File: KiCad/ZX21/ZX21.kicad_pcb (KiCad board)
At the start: 2 copper layers, 142 x 100 mm, 131 parts, among them IC1 ULA 2C210E, IC101 555, IC102 74HCT00, IC2 AT28C256, IC3 Z80A, IC301 3V3 PSU, IC302 ESP32-WROOM, IC303 AZ1117-3.3, IC4 62256, IC501 YM2149, IC502 GAL16V8, IC503 YMZ284, IC801 AS6C4008Extra, J1 Jack-DC, J101 Conn_01x03, J203 Conn_01x03, J204 Conn_01x03, J301 Conn_01x04, J302 Conn_01x03, J401 DB9_Male, J501 Conn_01x06, J502 Conn_01x08, J503 Conn_01x08, J504 Conn_01x08, J601 Conn_02x08_Odd_Even, J701 Conn_02x23_Row_Letter_First, J702 Conn_01x09, J703 Conn_01x09, X1 3.5MHz

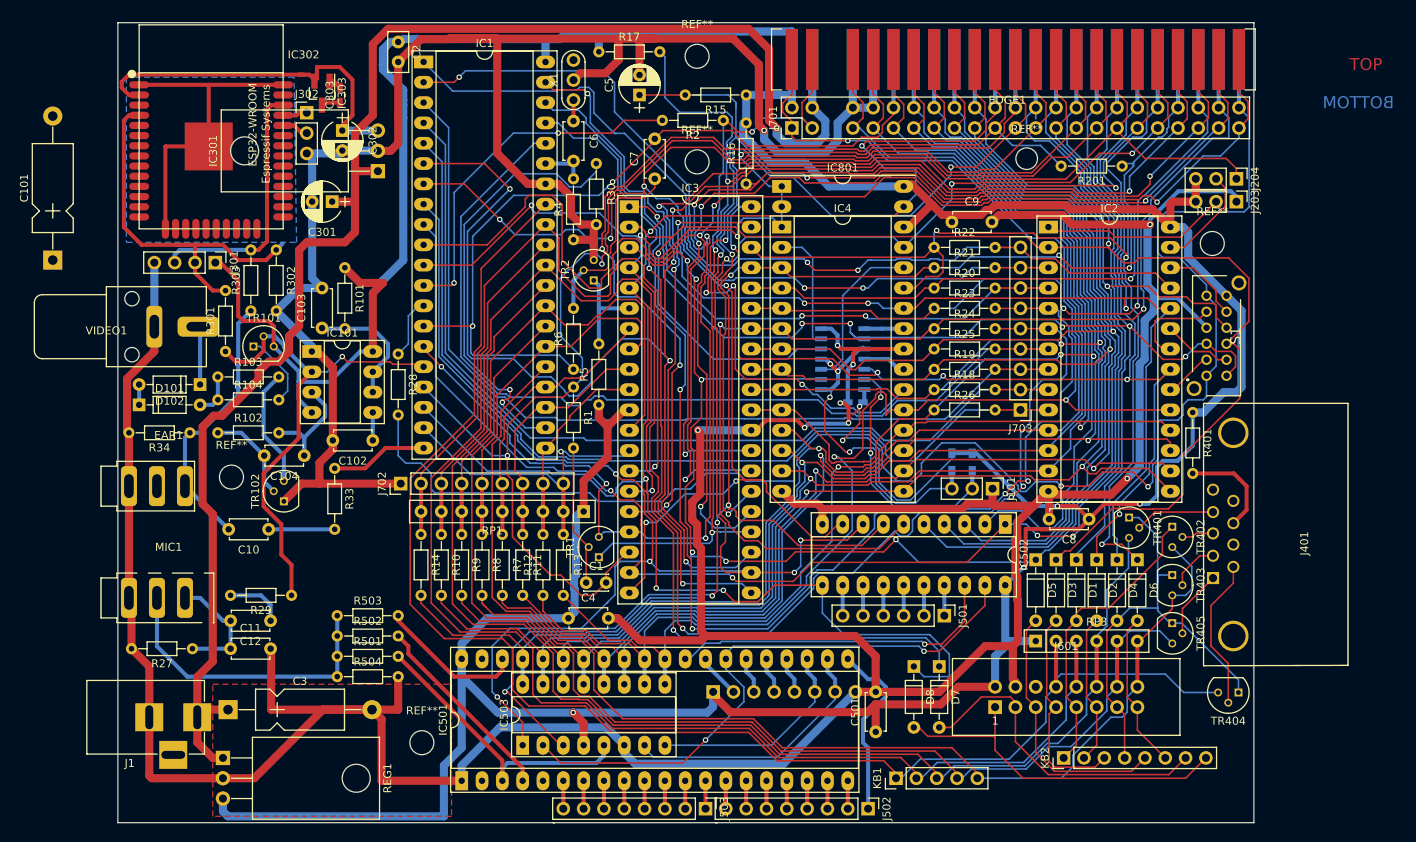
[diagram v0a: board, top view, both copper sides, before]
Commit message: ESP32 Flipped
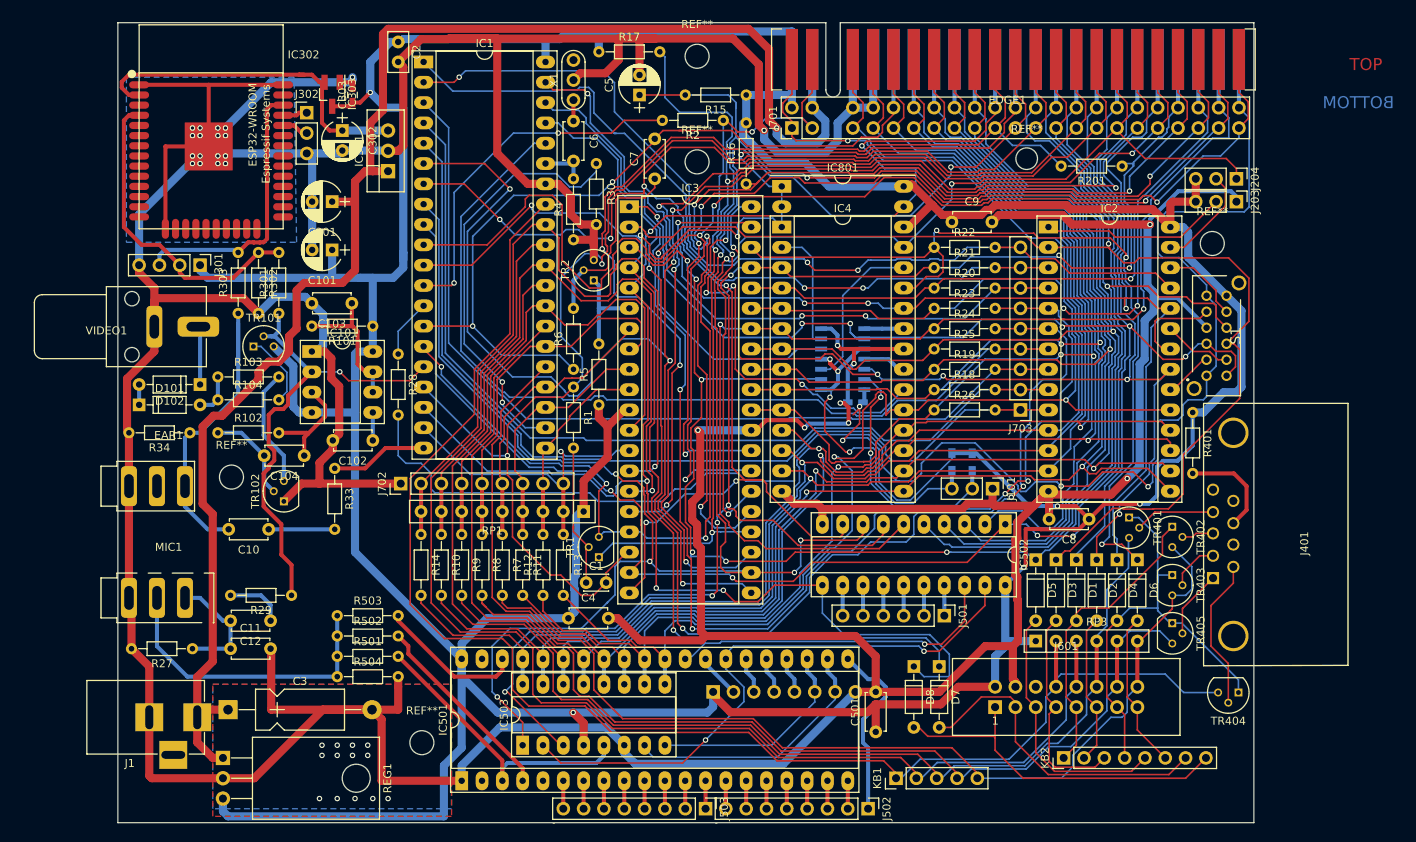
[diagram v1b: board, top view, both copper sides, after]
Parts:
- C101: footprint Capacitors_ThroughHole:CP_Axial_L11.0mm_D5.0mm_P18.00mm_Horizontal -> Capacitors_ThroughHole:CP_Radial_D5.0mm_P2.50mm
- IC301: footprint TO_SOT_Packages_THT:TO-220-3_Horizontal -> TO_SOT_Packages_THT:TO-220-3_Vertical
- moved C101 34.9 mm to (57.8, 65.4), turned to 180 degrees
- moved R301 8.19 mm to (51.1, 73.3)
- moved R101 8.09 mm to (62.9, 74.9), turned to 180 degrees
- moved C103 4.85 mm to (60.2, 72.1), turned to 180 degrees
- moved R302 2.25 mm to (48.6, 65.7)
- moved J301 1.93 mm to (41.3, 67.3)
- moved R303 1.62 mm to (46.0, 73.3)
- moved C303 1.59 mm to (60.3, 46.0)
- moved IC303 1.28 mm to (57.8, 46.0)
- moved IC301 1.27 mm to (64.8, 55.6)
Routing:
- net GND: track 775.2 -> 839.0 mm, vias 9 -> 39
- net +5V: track 562.4 -> 620.2 mm, vias 6 -> 7
- net VP: track 48.4 -> 39.4 mm
- net Net-(C103-Pad1): track 15.9 -> 22.8 mm
- net EAR_IN: track 33.8 -> 38.7 mm
- net TAPE_OUT: track 63.2 -> 59.9 mm
- net +3V3: track 47.1 -> 43.9 mm
- net A13: track 202.8 -> 200.1 mm
- net CLK: track 103.3 -> 101.0 mm
- net Net-(IC1-Pad22): track 54.7 -> 52.7 mm
- net Net-(C104-Pad1): track 15.5 -> 13.5 mm
- net RD: track 198.0 -> 196.4 mm
- net WR: track 265.3 -> 266.6 mm
- net IO22: track 33.0 -> 34.3 mm
- net D3: track 44.8 -> 45.9 mm
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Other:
- outline, holes or cut-outs redrawn
- rule trace_min: 0 -> 0.2032

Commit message: Gerbers made
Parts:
- added REF***: OSHW-Logo2_7.3x6mm_SilkScreen, Symbols:OSHW-Logo2_7.3x6mm_SilkScreen, F.Cu at (64.1, 63.8)
- added REF***: OSHW-Logo2_7.3x6mm_Copper, Symbols:OSHW-Logo2_7.3x6mm_Copper, F.Cu at (58.7, 105.1)
- moved R401 4.70 mm to (165.4, 90.4)
- moved TR402 0.57 mm to (162.8, 100.6)
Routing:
- net Net-(J401-Pad8): track 12.7 -> 6.90 mm
- net RD: track 196.4 -> 192.1 mm
- net A13: track 200.1 -> 203.8 mm, vias 7 -> 8
- net A14: track 203.6 -> 200.7 mm
- net INT: track 123.5 -> 125.3 mm
- net A0: track 138.5 -> 136.9 mm
- net A4': track 160.0 -> 158.5 mm
- net MREQ: track 187.4 -> 188.8 mm
- net A6': track 85.6 -> 84.2 mm
- net +5V: track 620.2 -> 619.1 mm, vias 7 -> 6
- net D2': track 173.2 -> 172.4 mm
- net D1': track 177.7 -> 176.9 mm
- net D0': track 186.3 -> 185.5 mm
- net A5': track 163.9 -> 163.2 mm
- net NMI: track 157.6 -> 158.4 mm
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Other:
- rule trace_min: 0.2032 -> 0
- board text added: "ZX21"
